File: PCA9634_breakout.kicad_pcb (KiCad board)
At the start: 2 copper layers, 35 x 40 mm, 27 parts, among them J1 Conn_01x05_Male, U1 PCA9634PW_118

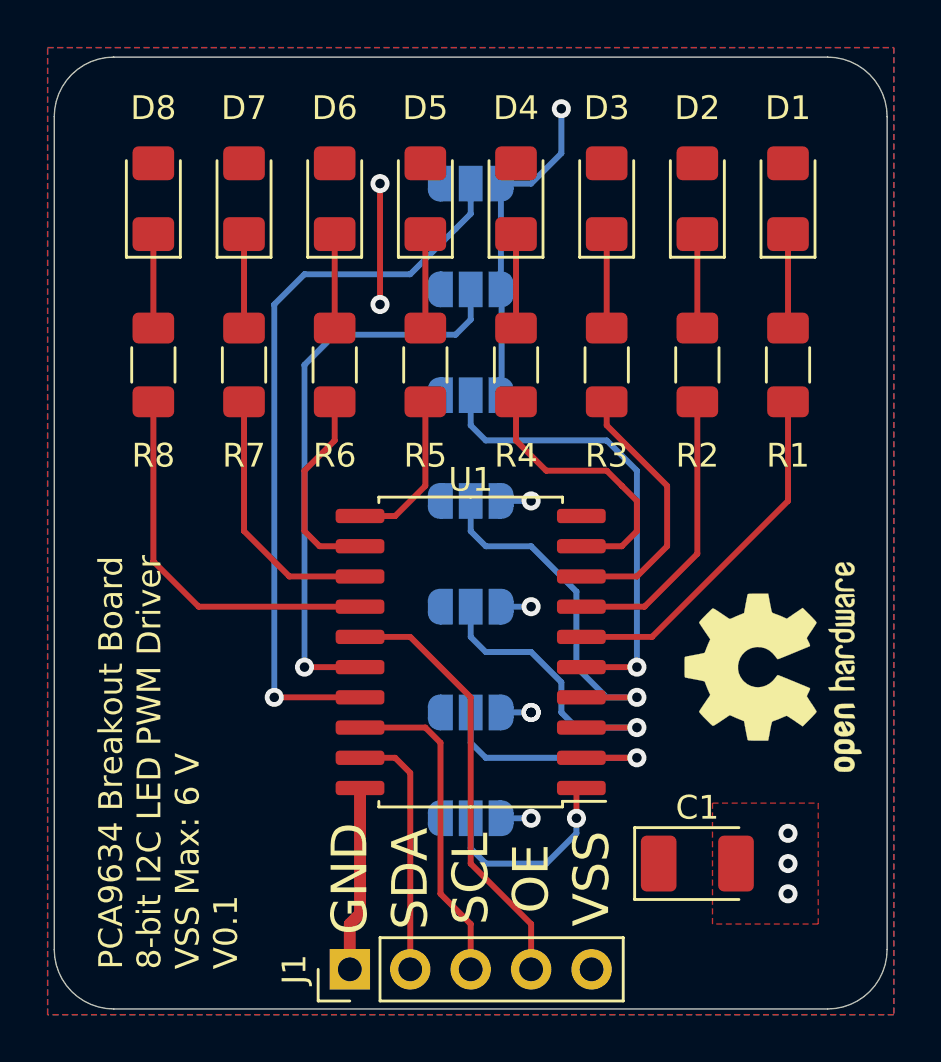
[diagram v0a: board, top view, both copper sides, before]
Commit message: feat: Changed footprints such that they are featured in the JLCPCB SMT assembly service as basic parts.
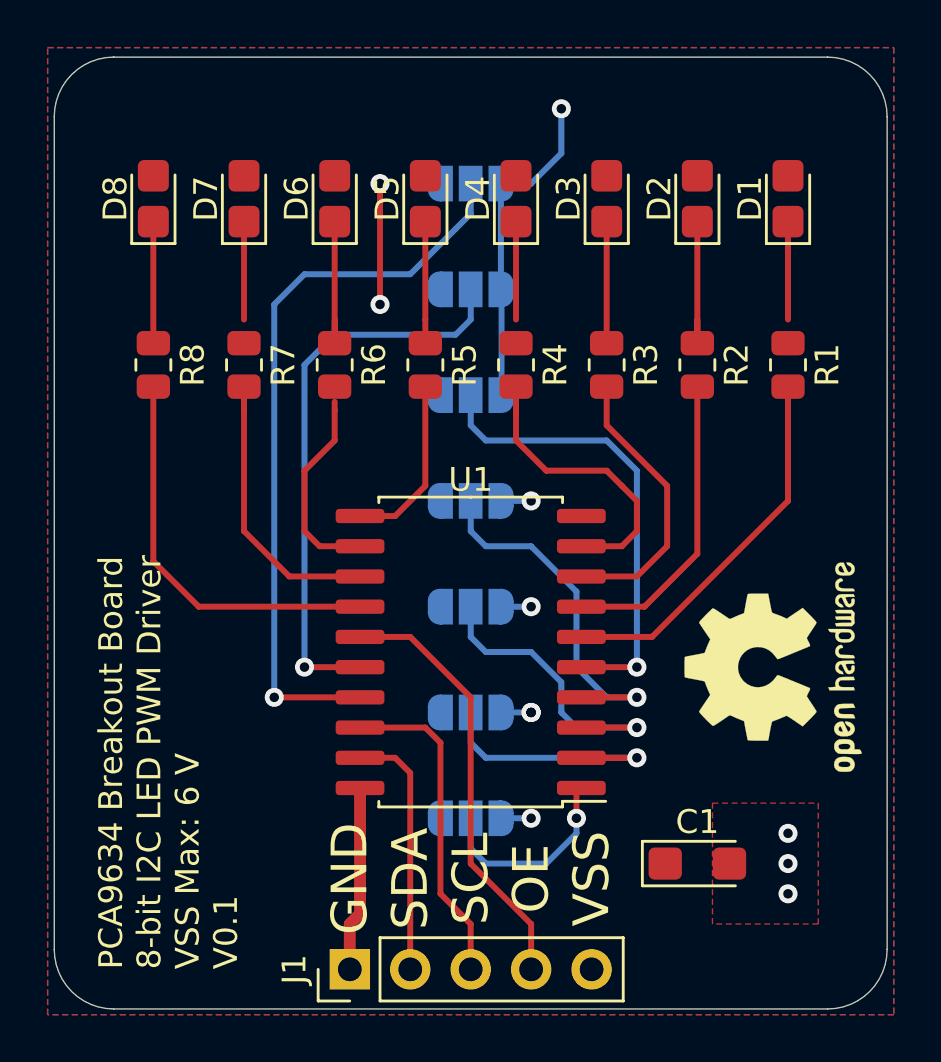
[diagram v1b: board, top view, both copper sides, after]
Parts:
- C1: value 47uF -> 10uF; footprint Capacitor_Tantalum_SMD:CP_EIA-3528-12_Kemet-T_Pad1.50x2.35mm_HandSolder -> Capacitor_Tantalum_SMD:CP_EIA-3216-18_Kemet-A
- D1, D2, D3, D4, D5, D6, D7, D8: footprint LED_SMD:LED_1206_3216Metric_Pad1.42x1.75mm_HandSolder -> LED_SMD:LED_0805_2012Metric_Castellated
- R1, R2, R3, R4, R5, R6, R7, R8: value 220 -> 150; footprint Resistor_SMD:R_1206_3216Metric_Pad1.30x1.75mm_HandSolder -> Resistor_SMD:R_0805_2012Metric

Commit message: changed solder jumper to double row pin 2.54 connector on top side
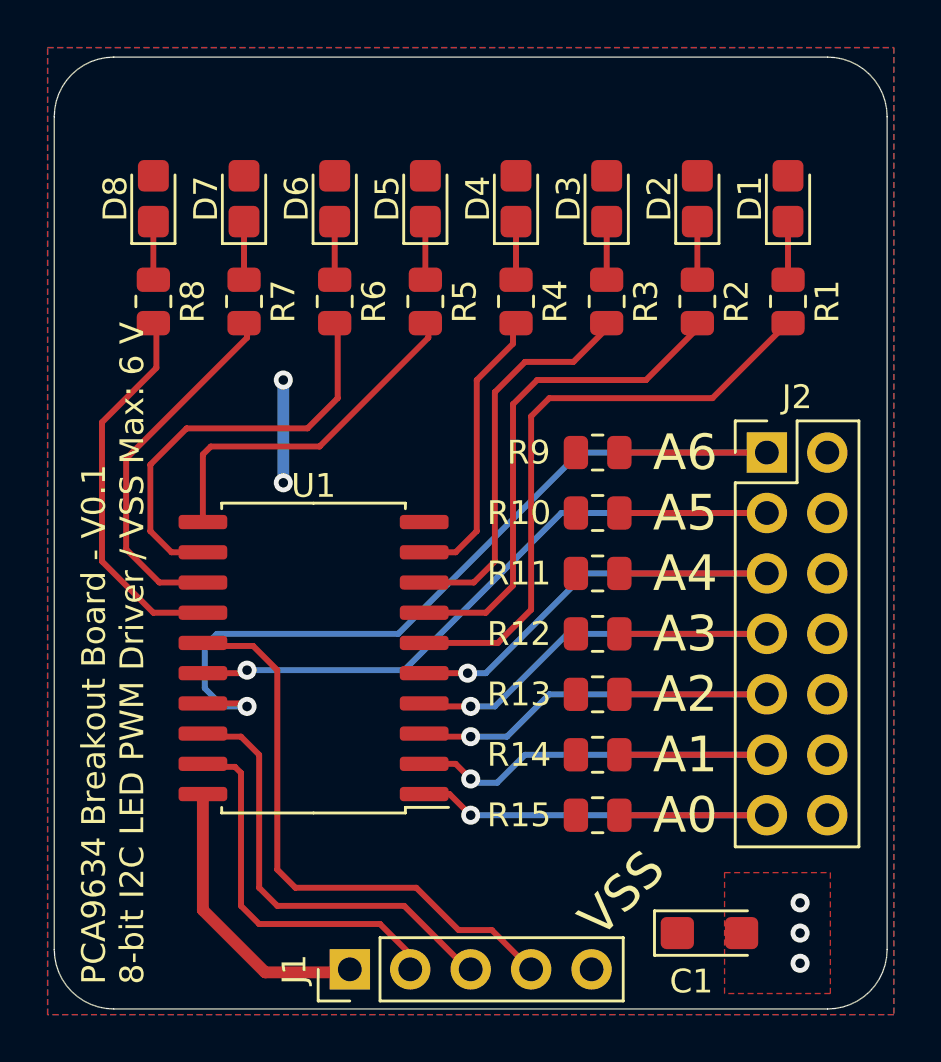
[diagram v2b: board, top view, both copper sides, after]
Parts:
- removed JP1, JP2, JP3, JP4, JP5, JP6, JP7: SolderJumper_3_Open, Jumper:SolderJumper-3_P1.3mm_Open_RoundedPad1.0x1.5mm
- removed REF**: OSHW-Logo2_9.8x8mm_SilkScreen, Symbol:OSHW-Logo2_9.8x8mm_SilkScreen
- added J2: Conn_02x07_Odd_Even, Connector_PinHeader_2.54mm:PinHeader_2x07_P2.54mm_Vertical, F.Cu at (178.2, 91.3)
- added R10: 10k, Resistor_SMD:R_0805_2012Metric, F.Cu at (171.1, 93.9)
- added R11: 10k, Resistor_SMD:R_0805_2012Metric, F.Cu at (171.1, 96.4)
- added R12: 10k, Resistor_SMD:R_0805_2012Metric, F.Cu at (171.1, 98.9)
- added R13: 10k, Resistor_SMD:R_0805_2012Metric, F.Cu at (171.1, 101.5)
- added R14: 10k, Resistor_SMD:R_0805_2012Metric, F.Cu at (171.1, 104.0)
- added R15: 10k, Resistor_SMD:R_0805_2012Metric, F.Cu at (171.1, 106.6)
- added R9: 10k, Resistor_SMD:R_0805_2012Metric, F.Cu at (171.1, 91.3)
- moved U1 6.61 mm to (159.1, 99.9)
- moved C1 2.96 mm to (175.8, 111.5)
- moved R1 2.67 mm to (179.1, 85.0)
- moved R2 2.67 mm to (175.3, 85.0)
- moved R3 2.67 mm to (171.4, 85.0)
- moved R4 2.67 mm to (167.6, 85.0)
- moved R5 2.67 mm to (163.8, 85.0)
- moved R6 2.67 mm to (160.0, 85.0)
- moved R7 2.67 mm to (156.2, 85.0)
- moved R8 2.67 mm to (152.4, 85.0)
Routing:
- net VSS: track 18.8 -> 4.32 mm, vias 6 -> 2
- net A0: track 8.41 -> 20.9 mm
- net A1: track 10.9 -> 21.7 mm
- net LED0: track 15.5 -> 25.4 mm
- net LED5: track 8.56 -> 17.4 mm
- net A5: track 24.3 -> 32.6 mm
- net LED1: track 12.5 -> 20.7 mm
- net A2: track 13.1 -> 21.3 mm
- net LED4: track 7.08 -> 14.9 mm
- net A6: track 31.4 -> 38.9 mm
- net OE: track 18.0 -> 24.3 mm
- net A3: track 15.5 -> 21.6 mm
- net SDA: track 10.4 -> 16.1 mm
- net LED2: track 11.5 -> 16.8 mm
- net SCL: track 14.8 -> 19.0 mm
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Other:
- board text added: "PCA9634 Breakout Board - V0.1 8-bit I2C LED PWM Driver / VSS Max: 6 V"
- board text removed: "GND"
- board text removed: "OE"
- board text removed: "PCA9634 Breakout Board 8-bit I2C LED PWM Driver VSS Max: 6 V V0.1"
- board text removed: "SCL"
- board text removed: "SDA"

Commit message: converted to 4 layer pcb
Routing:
- net VSS: track 4.32 -> 39.9 mm, vias 2 -> 15
- net LED2: track 16.8 -> 21.4 mm
- net LED3: track 11.8 -> 16.2 mm, vias 0 -> 2
- net LED0: track 25.4 -> 24.5 mm
- net A4: track 22.0 -> 22.7 mm
- net LED1: track 20.7 -> 20.1 mm
- added copper zone on GND, net GND
- added copper zone on PWR, net VSS
- removed copper zone on B.Cu, net GND
- removed copper zone on F.Cu, net VSS
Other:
- copper layers 2 -> 4
- board text added: "PCA9634 Breakout Board - V0.2 8-bit I2C LED PWM Driver"
- board text removed: "PCA9634 Breakout Board - V0.1 8-bit I2C LED PWM Driver / VSS Max: 6 V"
